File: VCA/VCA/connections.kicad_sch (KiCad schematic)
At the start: 12 parts, among them J10 Conn_01x03, J11 Conn_01x03, J12 Conn_01x03, J13 Conn_01x02, J13 Conn_02x05_Odd_Even, J14 Conn_01x03, J15 Conn_01x03, J16 Conn_01x02

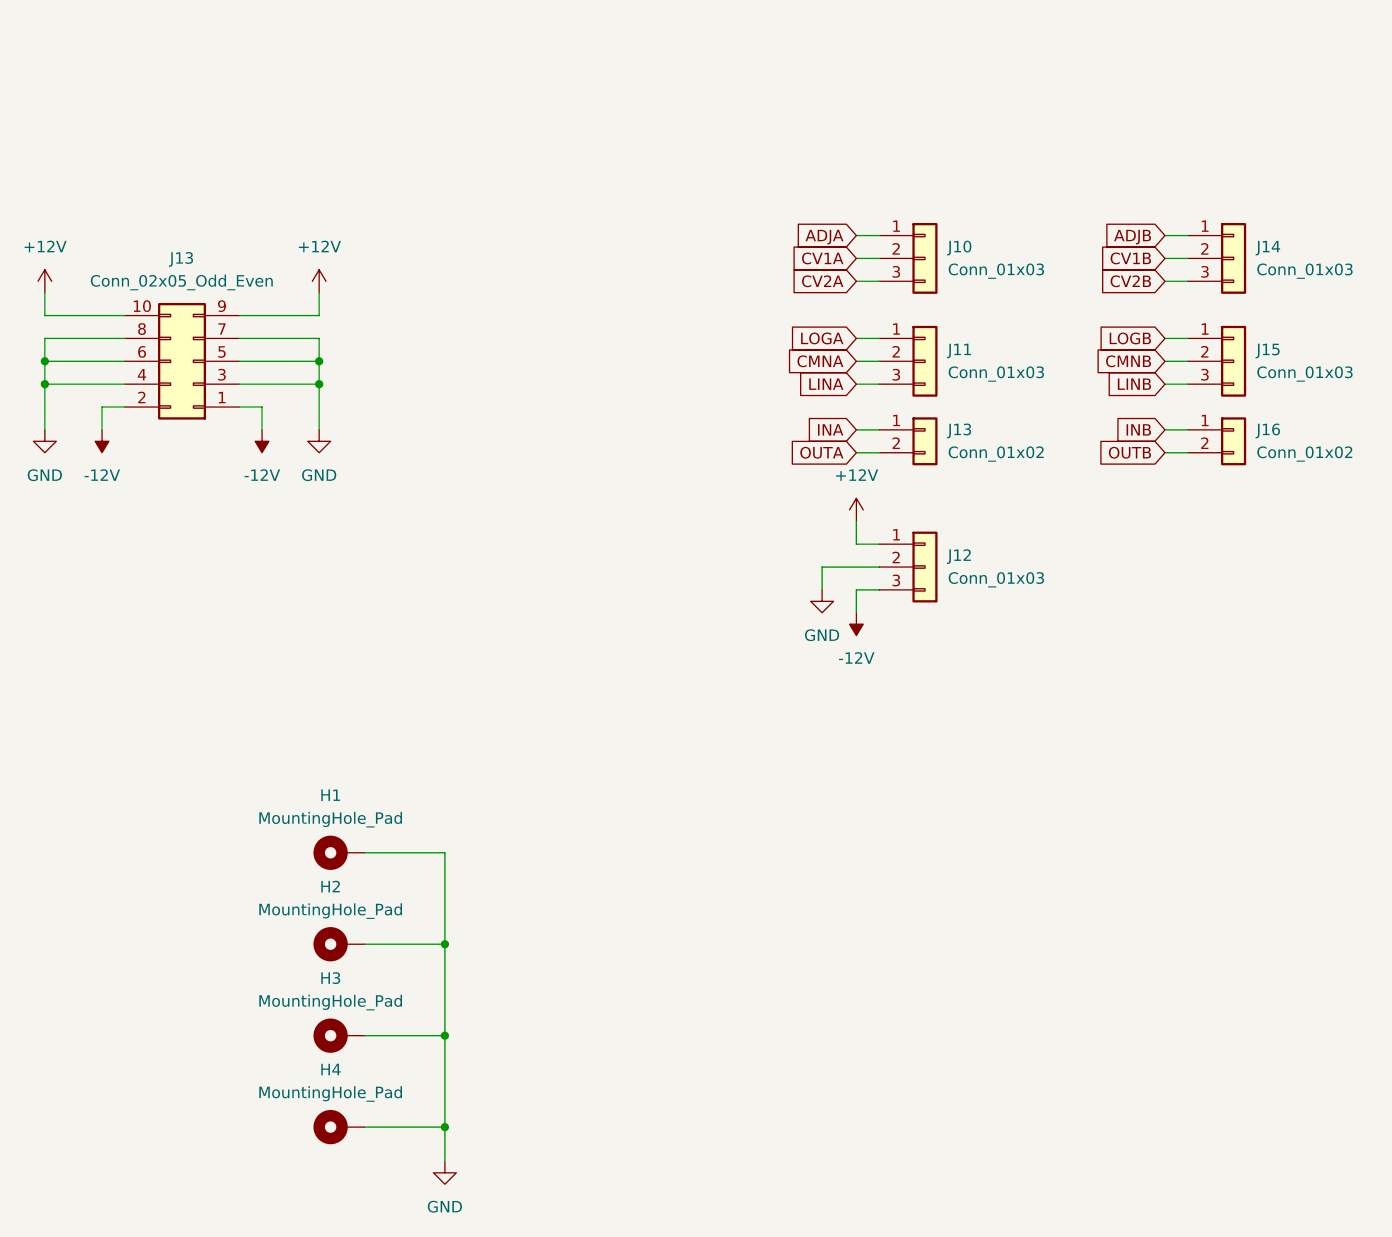
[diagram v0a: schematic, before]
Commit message: VCA - correct resistors sizes
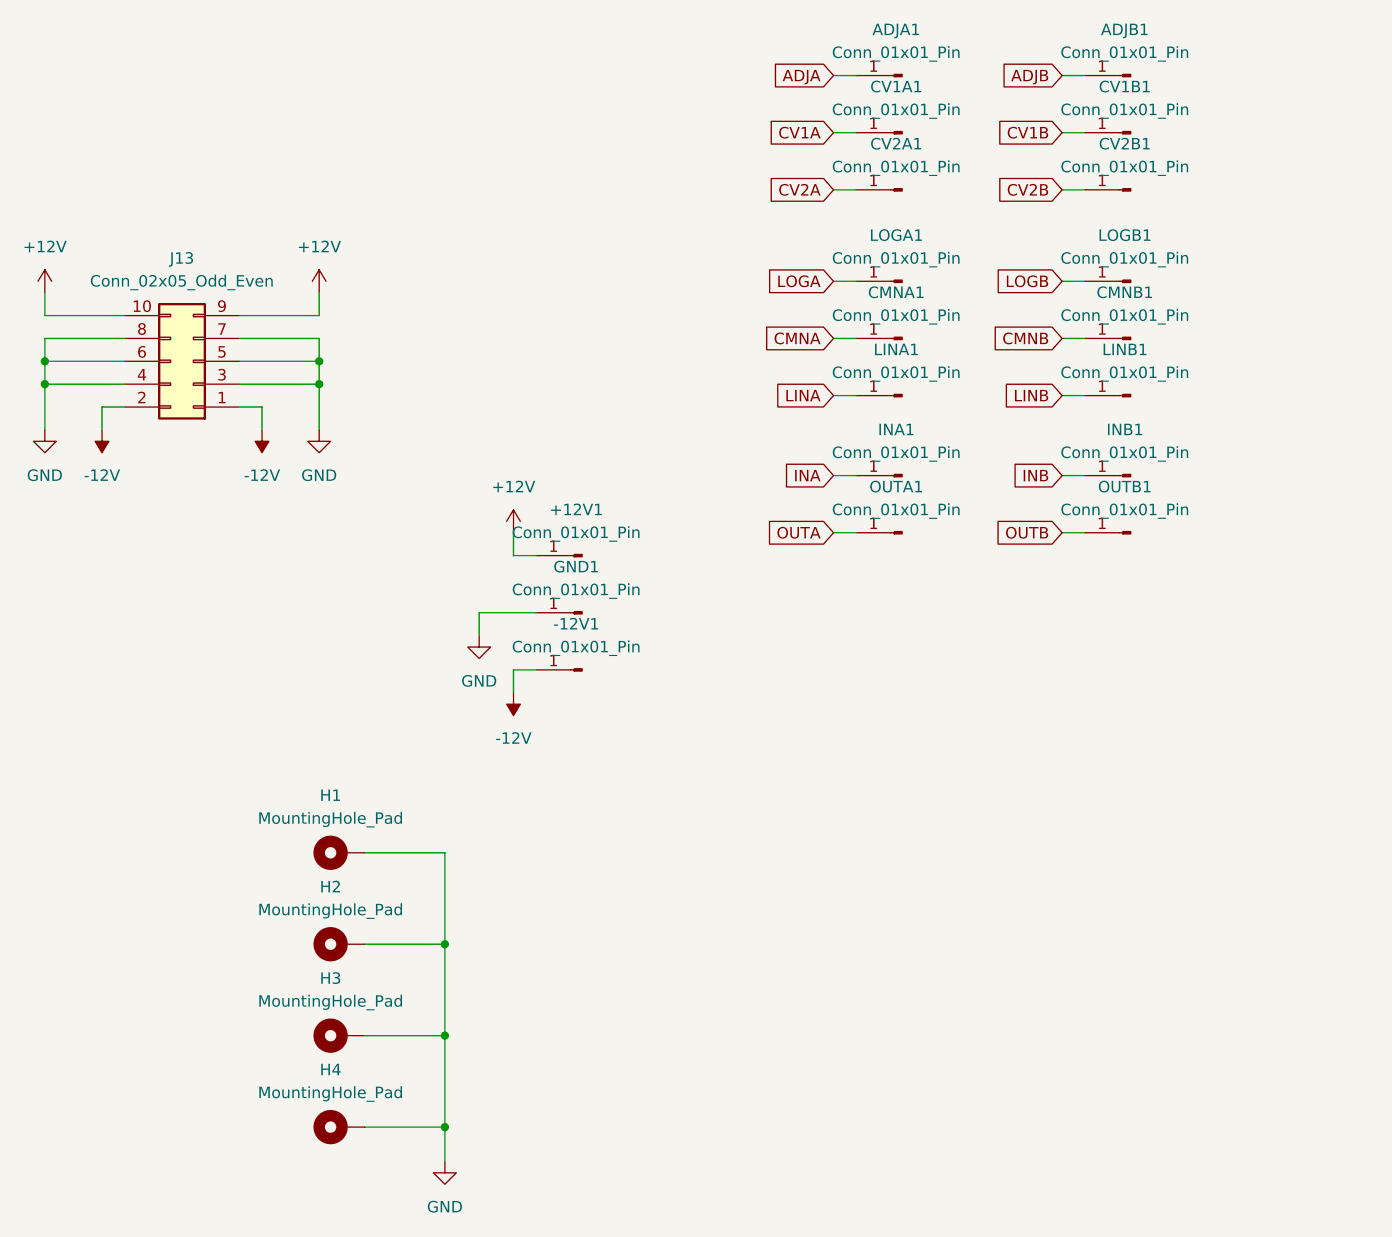
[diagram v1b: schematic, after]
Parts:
- removed J10, J11, J12, J14, J15: Conn_01x03, Connector_PinHeader_2.54mm:PinHeader_1x03_P2.54mm_Vertical, symbol Connector_Generic:Conn_01x03
- removed J13, J16: Conn_01x02, Connector_PinHeader_2.54mm:PinHeader_1x02_P2.54mm_Vertical, symbol Connector_Generic:Conn_01x02
- added +12V1, -12V1, ADJA1, ADJB1, CMNA1, CMNB1, CV1A1, CV1B1, CV2A1, CV2B1, GND1, INA1, INB1, LINA1, LINB1, LOGA1, LOGB1, OUTA1, OUTB1: Conn_01x01_Pin, Connector_Pin:Pin_D1.0mm_L10.0mm, symbol Connector:Conn_01x01_Pin
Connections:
- net +12V: now also +12V1.1 (Pin_1)
- net -12V: now also -12V1.1 (Pin_1)
- net ADJA: now also ADJA1.1 (Pin_1)
- net ADJB: now also ADJB1.1 (Pin_1)
- net CMNA: now also CMNA1.1 (Pin_1)
- net CMNB: now also CMNB1.1 (Pin_1)
- net CV1A: now also CV1A1.1 (Pin_1)
- net CV1B: now also CV1B1.1 (Pin_1)
- net CV2A: now also CV2A1.1 (Pin_1)
- net CV2B: now also CV2B1.1 (Pin_1)
- net GND: now also GND1.1 (Pin_1)
- net INA: now also INA1.1 (Pin_1)
- net INB: now also INB1.1 (Pin_1)
- net LINA: now also LINA1.1 (Pin_1)
- net LINB: now also LINB1.1 (Pin_1)
- net LOGA: now also LOGA1.1 (Pin_1)
- net LOGB: now also LOGB1.1 (Pin_1)
- net OUTA: now also OUTA1.1 (Pin_1)
- net OUTB: now also OUTB1.1 (Pin_1)
